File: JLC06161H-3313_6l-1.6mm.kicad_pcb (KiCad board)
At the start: 6 copper layers, 24 x 24 mm, 0 parts

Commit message: add default zone
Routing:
- added copper zone on F.Cu, net (none)
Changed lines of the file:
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@@
 		(layer "Edge.Cuts")
 	)
+	(zone
+		(net 0)
+		(net_name "")
+		(layer "F.Cu")
+		(hatch edge 0.5)
+		(connect_pads
+			(clearance 0.127)
+		)
+		(min_thickness 0.127)
+		(filled_areas_thickness no)
+		(fill
+			(thermal_gap 0.127)
+			(thermal_bridge_width 0.5)
+			(smoothing fillet)
+			(radius 1)
+			(island_removal_mode 1)
+			(island_area_min 10)
+		)
+		(polygon
+			(pts
+				(xy 29 29) (xy 55 29) (xy 55 55) (xy 29 55)
+			)
+		)
+	)
 )

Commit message: update
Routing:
- added copper zone on B.Cu, net (none)
- added copper zone on In1.Cu, net (none)
- added copper zone on In2.Cu, net (none)
- added copper zone on In3.Cu, net (none)
- added copper zone on In4.Cu, net (none)
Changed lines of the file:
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@@
 		(net 0)
 		(net_name "")
-		(layer "F.Cu")
+		(layers "F&B.Cu")
 		(hatch edge 0.5)
 		(connect_pads
@@
 			)
 		)
+	)
+	(zone
+		(net 0)
+		(net_name "")
+		(layers "In1.Cu" "In2.Cu" "In3.Cu" "In4.Cu")
+		(hatch edge 0.5)
+		(priority 1)
+		(connect_pads
+			(clearance 0.2)
+		)
+		(min_thickness 0.2)
+		(filled_areas_thickness no)
+		(fill
+			(thermal_gap 0.2)
+			(thermal_bridge_width 0.5)
+			(smoothing fillet)
+			(radius 1)
+			(island_removal_mode 1)
+			(island_area_min 10)
+		)
+		(polygon
+			(pts
+				(xy 28 28) (xy 56 28) (xy 56 56) (xy 28 56)
+			)
+		)

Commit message: update silk
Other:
- board text added: "JLCJLCJLCJLC"
- board text added: "TES"
- board text added: "VERV"
- board text added: "test test test"
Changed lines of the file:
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@@
 	)
 	(net 0 "")
+	(gr_rect
+		(start 37 40)
+		(end 42 45)
+		(stroke
+			(width 0.1)
+			(type solid)
+		)
+		(fill solid)
+		(layer "F.SilkS")
+	)
+	(gr_line
+		(start 48 35.875)
+		(end 45.75 35.874999)
+		(stroke
+			(width 0.1)
+			(type default)
+		)
+		(layer "F.SilkS")
+	)
+	(gr_line
+		(start 45.75 35.874999)
+		(end 45.750001 38.124998)
+		(stroke
+			(width 0.1)
+			(type default)
+		)
+		(layer "F.SilkS")
+	)
+	(gr_line
+		(start 47.999999 38.124999)
+		(end 48 35.875)
+		(stroke
+			(width 0.1)
+			(type default)
+		)
+		(layer "F.SilkS")
+	)
+	(gr_line
+		(start 47.999999 38.124999)
+		(end 45.750001 38.124998)
+		(stroke
+			(width 0.1)
+			(type default)
+		)
+		(layer "F.SilkS")
+	)
 	(gr_line
 		(start 30 31)
@@
 		)
 		(layer "Edge.Cuts")
+	)
+	(gr_text "TES"
+		(at 36.75 36.5 0)
+		(layer "F.SilkS")
+		(effects
+			(font
+				(size 1 1)
+				(thickness 0.2)
+				(bold yes)
+				(italic yes)
+			)
+			(justify left)
+		)
+	)
+	(gr_text "VERV"
+		(at 45 36.624999 0)
+		(layer "F.SilkS")
+		(effects
+			(font
+				(size 0.8 0.8)
+				(thickness 0.15)
+				(bold yes)
+				(italic yes)
+			)
+			(justify right)
+		)
+	)
+	(gr_text "test test test"
+		(at 36.75 37.749999 0)
+		(layer "F.SilkS")
+		(effects
+			(font
+				(size 0.8 0.8)
+				(thickness 0.15)
+				(bold yes)
+			)
+			(justify left)
+		)
+	)
+	(gr_text "JLCJLCJLCJLC"
+		(at 42 46 0)
+		(layer "F.SilkS")
+		(effects
+			(font
+				(size 0.8 0.8)
+				(thickness 0.15)
+			)
+		)
+	)
+	(dimension
+		(type aligned)
+		(layer "Dwgs.User")
+		(pts
+			(xy 49.999999 54.000001) (xy 50 30)
+		)
+		(height 7.999999)
+		(gr_text "24,0000 mm"
+			(at 56.849999 42 89.99999523)
+			(layer "Dwgs.User")
+			(effects
+				(font
+					(size 1 1)
+					(thickness 0.15)
+				)
+			)
+		)
+		(format
+			(prefix "")
+			(suffix "")
+			(units 3)
+			(units_format 1)
+			(precision 4)
+		)
+		(style
+			(thickness 0.1)
+			(arrow_length 1.27)
+			(text_position_mode 0)
+			(extension_height 0.58642)
+			(extension_offset 0.5) keep_text_aligned)
+	)
+	(dimension
+		(type aligned)
+		(layer "Dwgs.User")
+		(pts
+			(xy 30 50) (xy 54 50)
+		)
+		(height 7.999999)
+		(gr_text "24,0000 mm"
+			(at 42 56.849999 0)
+			(layer "Dwgs.User")
+			(effects
+				(font
+					(size 1 1)
+					(thickness 0.15)
+				)
+			)
+		)
+		(format
+			(prefix "")
+			(suffix "")
+			(units 3)
+			(units_format 1)
+			(precision 4)
+		)
+		(style
+			(thickness 0.1)
+			(arrow_length 1.27)
+			(text_position_mode 0)
+			(extension_height 0.58642)
+			(extension_offset 0.5) keep_text_aligned)
 	)
 	(zone
@@
 		)
 	)
+	(group ""
+		(members "2b3a430e-1fa6-4240-9822-121789126b80" "6edb1cfc-a614-47a0-8cb0-bb82824a9954"
+			"ad4880dd-f1f2-429d-bf37-3f960fe342ef"
+		)
+	)
+	(group ""
+		(members "026c03b3-14e4-41ea-b695-ffe4874080d9")
+	)
+	(group ""
+		(members "61bea4c9-d85d-4408-af02-c35b8adabee3" "93881c84-3ea3-43d2-a201-6c500d60c2c2"
+			"b1573c85-3812-4e94-9812-3783792db5f0" "d972b3f0-d61c-492a-9298-391b19a5217e"
+		)
+	)

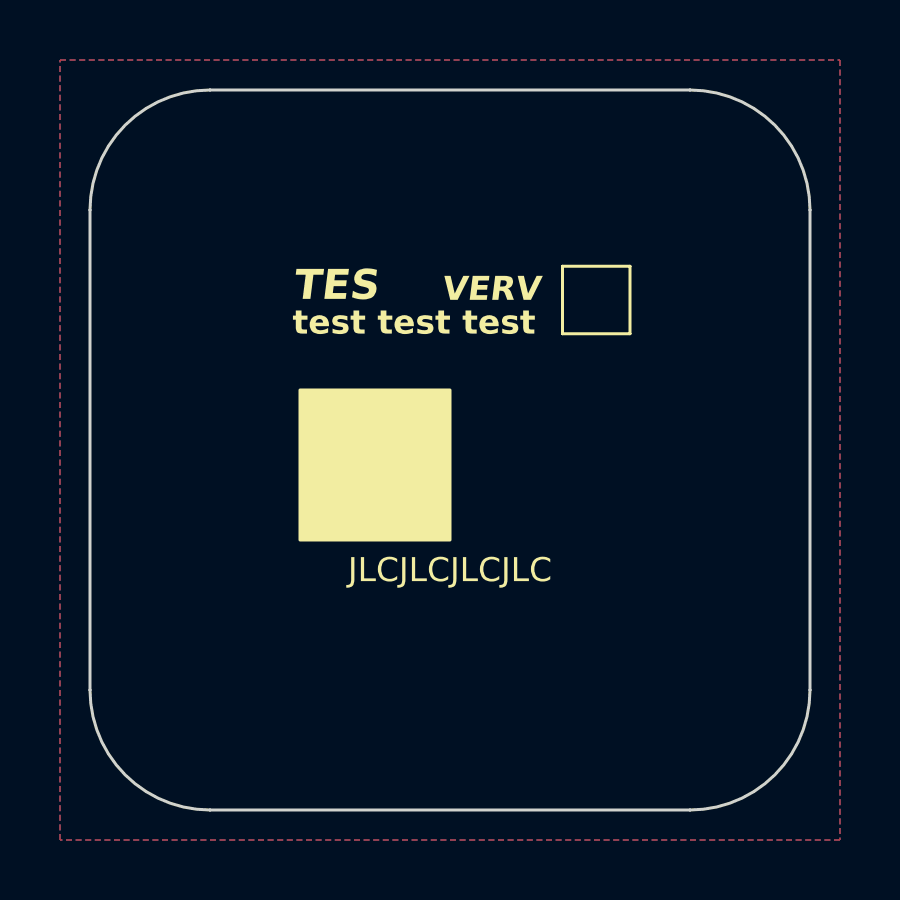
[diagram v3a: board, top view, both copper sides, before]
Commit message: Update to kicad9
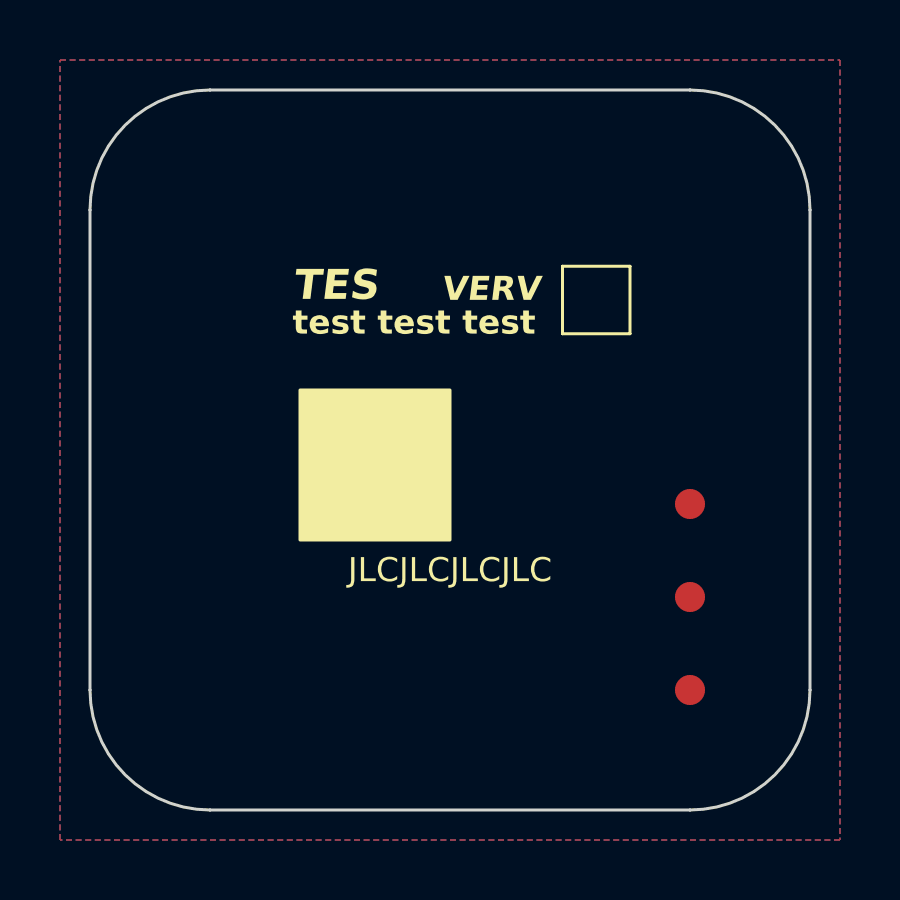
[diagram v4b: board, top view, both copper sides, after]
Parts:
- added FID1: Fiducial, MAS_Package_std:Fiducial_1mm_Mask2mm, F.Cu at (50.0, 43.8)
- added FID2: Fiducial, MAS_Package_std:Fiducial_1mm_Mask2mm, F.Cu at (50.0, 46.9)
- added FID3: Fiducial, MAS_Package_std:Fiducial_1mm_Mask2mm, F.Cu at (50.0, 50.0)
